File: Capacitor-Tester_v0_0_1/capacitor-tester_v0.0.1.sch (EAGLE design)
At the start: 30 parts, among them IC1 AD8531ARZ, IC2 MC34063EBD-TR, J1 USB4125-GF-A-0190_REVA2, J2 DS1044-140G, J3 250-102, U1 AD5933, U2 LM6171AIMX/NOPB, Y1 LFSPXO018034

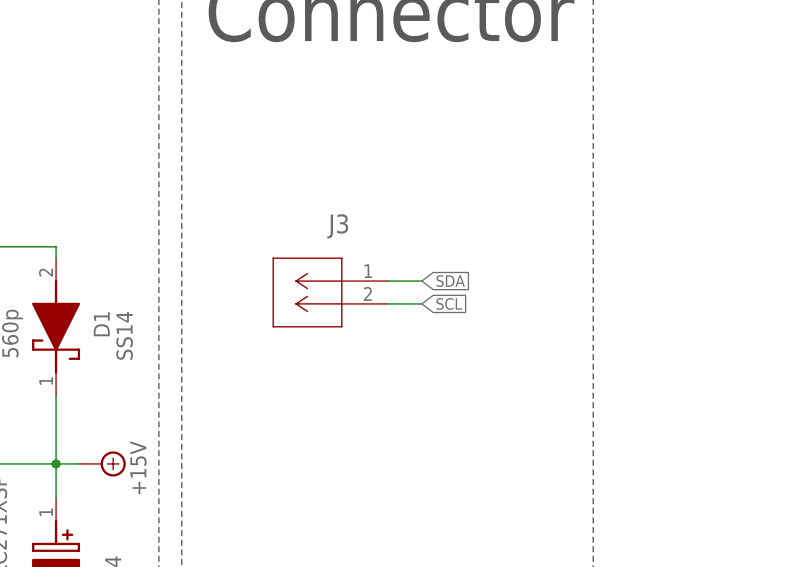
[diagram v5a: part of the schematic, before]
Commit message: v0.0.1 - Changed wago 250-102 for 250-103 and connected FUNC_GEN to the input connector
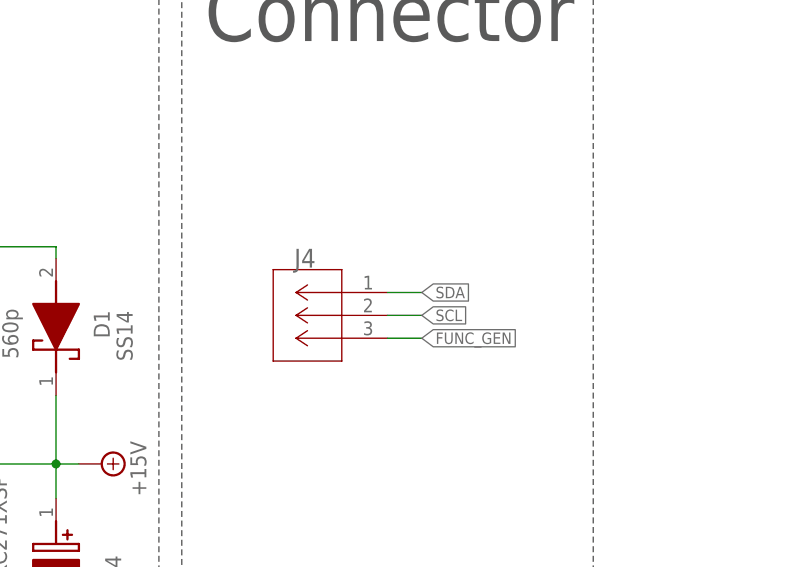
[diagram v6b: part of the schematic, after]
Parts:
- removed J3: 250-102, custom_library:250-102
- added J4: 250-103, custom_library:250-103
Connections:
- net FUNC_GEN: now also J4.3
- net SCL: now also J4.2; no longer J3.2
- net SDA: now also J4.1; no longer J3.1
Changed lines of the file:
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@@
 <part name="SUPPLY12" library="supply2" library_urn="urn:adsk.eagle:library:372" deviceset="+5V" device=""/>
 <part name="SUPPLY10" library="supply2" library_urn="urn:adsk.eagle:library:372" deviceset="+15V" device=""/>
-<part name="J3" library="custom_library" deviceset="250-102" device=""/>
+<part name="J4" library="custom_library" deviceset="250-103" device=""/>
 </parts>
 <sheets>
@@
 <attribute name="VALUE" x="41.91" y="-33.655" size="1.778" layer="96"/>
 </instance>
-<instance part="J3" gate="A" x="87.63" y="119.38" smashed="yes" rot="MR0">
-<attribute name="NAME" x="83.4644" y="124.6886" size="2.0828" layer="95" ratio="6" rot="SMR0"/>
+<instance part="J4" gate="A" x="87.63" y="118.11" smashed="yes" rot="MR0">
+<attribute name="NAME" x="79.6544" y="120.8786" size="2.0828" layer="95" ratio="6" rot="SMR0"/>
 </instance>
 </instances>
@@
 </segment>
 <segment>
-<pinref part="J3" gate="A" pin="2"/>
-<wire x1="87.63" y1="116.84" x2="91.44" y2="116.84" width="0.1524" layer="91"/>
-<label x="91.44" y="116.84" size="1.27" layer="95" rot="MR180" xref="yes"/>
+<pinref part="J4" gate="A" pin="2"/>
+<wire x1="87.63" y1="115.57" x2="91.44" y2="115.57" width="0.1524" layer="91"/>
+<label x="91.44" y="115.57" size="1.27" layer="95" xref="yes"/>
 </segment>
 </net>
@@
 </segment>
 <segment>
-<pinref part="J3" gate="A" pin="1"/>
-<wire x1="87.63" y1="119.38" x2="91.44" y2="119.38" width="0.1524" layer="91"/>
-<label x="91.44" y="119.38" size="1.27" layer="95" rot="MR180" xref="yes"/>
+<pinref part="J4" gate="A" pin="1"/>
+<wire x1="87.63" y1="118.11" x2="91.44" y2="118.11" width="0.1524" layer="91"/>
+<label x="91.44" y="118.11" size="1.27" layer="95" xref="yes"/>
 </segment>
 </net>
@@
 <label x="-55.88" y="11.43" size="1.27" layer="95" rot="R270" xref="yes"/>
 </segment>
-</net>
+<segment>
+<pinref part="J4" gate="A" pin="3"/>
+<wire x1="87.63" y1="113.03" x2="91.44" y2="113.03" width="0.1524" layer="91"/>
+<label x="91.44" y="113.03" size="1.27" layer="95" xref="yes"/>
+</segment>
+</net>

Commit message: v0.0.1 - Version control. Added DAC6571
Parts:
- added C7: 1u, custom_library:CAPACITOR_SMD_CERAMIC0603
- added C8: 10u, custom_library:CAPACITOR_SMD_CERAMIC0603
- added IC3: DAC6571IDBVT, DAC6571IDBVT:DAC6571IDBVT
- added IC4: AD8531ARZ, AD8531ARZ:AD8531ARZ
- added R13, R15, R16: 20k-1%, custom_library:RESISTOR_SMD0603
- added R14: 4k-1%, custom_library:RESISTOR_SMD0603
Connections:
- new net DAC_OUT: IC3.VOUT
- new net N$12: C7.1, IC4.+IN_A, R15.2, R16.1
- new net N$9: IC4.-IN_A, R13.1, R14.1
- net +5V: now also C8.1, IC3.VDD, IC4.V+, R15.1
- net GND: now also C7.2, C8.2, IC3.A0, IC3.GND, IC4.V-, R16.2
- net OPAMP_OUT: now also IC4.OUT_A, R14.2
- net SCL: now also IC3.SCL
- net SDA: now also IC3.SDA
- net VOUT: now also R13.2
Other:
- note added: "DAC6571"
- note added: "OPAMP UZA AD8531"
- note added: "OPAMP UZB AD8531"
- note removed: "OPAMP AD8531"

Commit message: v0.0.1 - Version control before big changes in the schematic
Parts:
- removed C3, C7: 1u, custom_library:CAPACITOR_SMD_CERAMIC0603
- removed R15, R16, R5, R6: 20k-1%, custom_library:RESISTOR_SMD0603
- R13: value 20k-1% -> 5k-1%
- R14: value 4k-1% -> 10k-1%
- R2: value 20k-1% -> 10k-1%
- R4: value 4k-1% -> 1k-1%
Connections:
- removed net N$12: C7.1, IC4.+IN_A, R15.2, R16.1
- removed net N$4: C3.1, IC1.+IN_A, R5.2, R6.1
- removed net OPAMP_OUT: IC1.OUT_A, IC4.OUT_A, J2.1, J2.2, J2.3, J2.4, J2.5, J2.6, J2.7, R14.2, R4.2
- new net UZA_OUT: IC1.OUT_A, J2.1, J2.2, J2.3, J2.4, J2.5, J2.6, J2.7, R4.2
- new net UZB_OUT: IC1.+IN_A, IC4.OUT_A, R14.2
- net +5V: no longer R15.1, R5.1
- net DAC_OUT: now also IC4.+IN_A
- net GND: now also R13.2; no longer C3.2, C7.2, R16.2, R6.2
- net VOUT: no longer R13.2
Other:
- moved on the sheet: IC1, IC4, R13, R14, R2, R4
